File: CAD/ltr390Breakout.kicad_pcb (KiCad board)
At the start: 2 copper layers, 12.7 x 12.7 mm, 7 parts, among them J1 Conn_01x04_Male, U1 LTR390

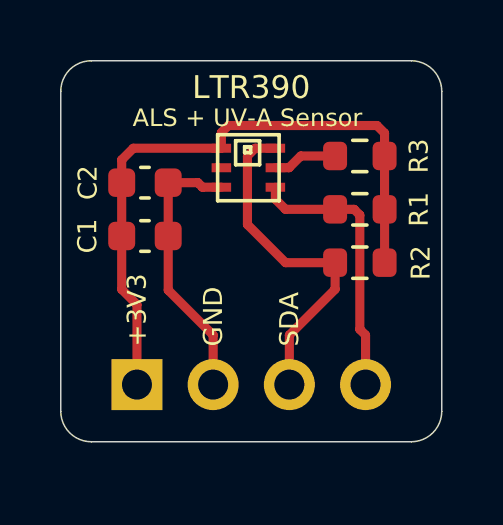
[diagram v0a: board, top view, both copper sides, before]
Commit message: added castellated holes
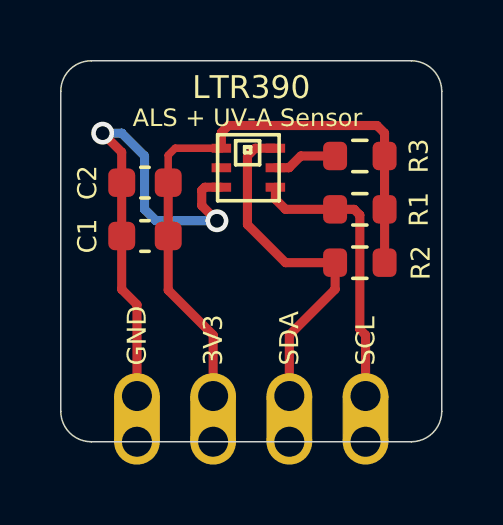
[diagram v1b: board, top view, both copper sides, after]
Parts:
- J1: value Conn_01x04_Male -> Castellated_Conn_01x04; footprint Connector_PinHeader_2.54mm:PinHeader_1x04_P2.54mm_Vertical -> DS-connectors:Castellated_PinHeader_01x04_P2.54mm_Vertical
- moved J1 2.57 mm to (132.1, 103.9)
- turned C1 to 180 degrees
- turned C2 to 180 degrees
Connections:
- J1 pad 1: +3V3 -> GND
- J1 pad 2: GND -> +3V3
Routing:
- net GND: track 9.19 -> 17.2 mm, vias 0 -> 2
- net +3V3: track 21.7 -> 21.0 mm
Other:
- board text added: "3V3"
- board text added: "SCL"
- board text removed: "+3V3"
